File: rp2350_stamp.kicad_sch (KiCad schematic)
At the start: 43 parts, among them J1 Conn_West, J2 Conn_North, J3 Conn_South, J4 Conn_East, Q1 BSS84, SW1 SW_RESET, SW2 SW_BOOTSEL, U1 W25Q128JVPIQ, U2 ME4055, U3 AP2112K-3.3, U4 RP235x-A, Y1 XYDBPCNANF-12MHZ

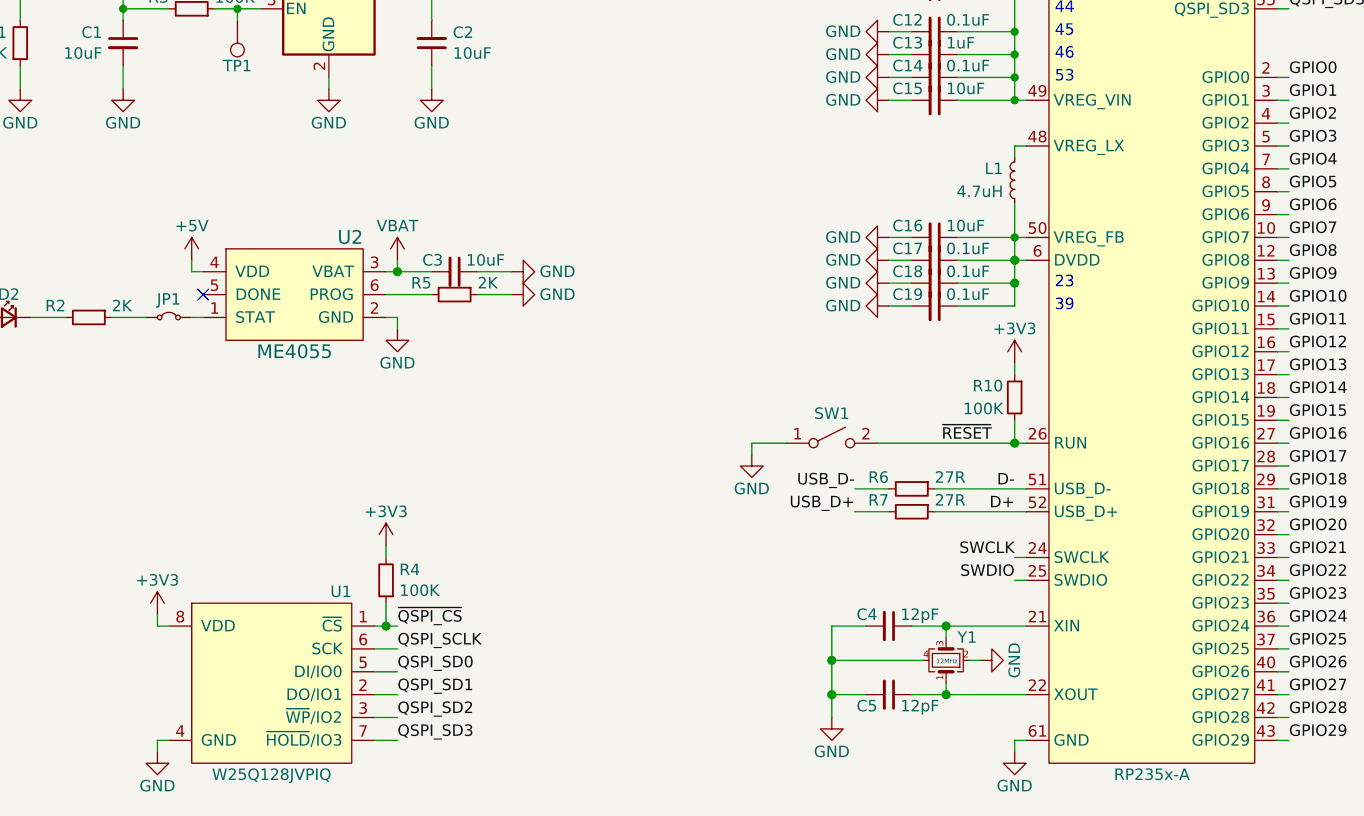
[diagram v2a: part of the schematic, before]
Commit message: Rev 4
- Put chip name on the board
- Fixup pin markers to be uniform
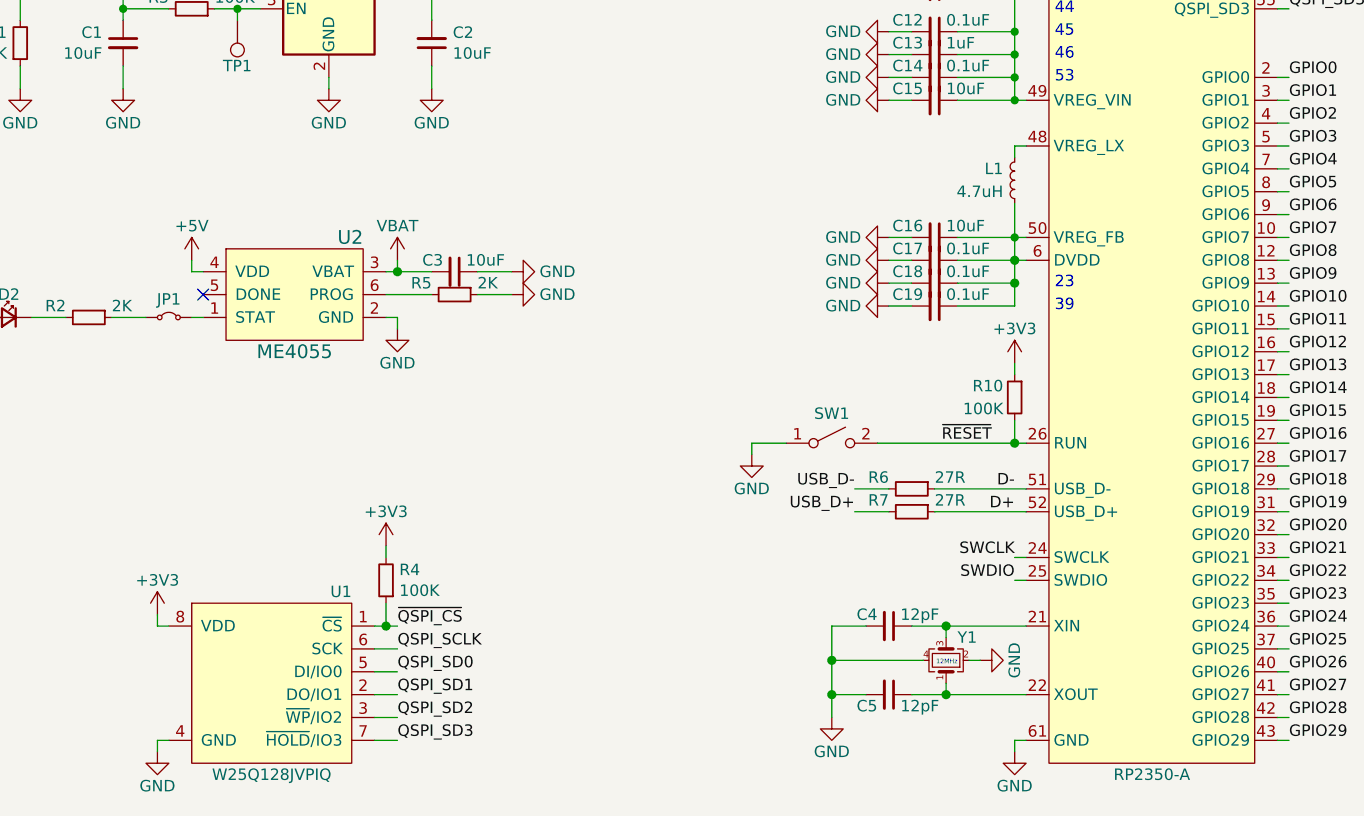
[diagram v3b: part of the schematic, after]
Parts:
- U4: value RP235x-A -> RP2350-A
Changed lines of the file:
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@@
 (kicad_sch
-	(version 20231120)
+	(version 20240602)
 	(generator "eeschema")
-	(generator_version "8.0")
+	(generator_version "8.99")
 	(paper "A4")
 	(title_block
 		(title "RP2350 Stamp")
 	)
+	(text "53"
+		(exclude_from_sim no)
+		(at 146.685 78.74 0)
+		(effects
+			(font
+				(size 1.27 1.27)
+			)
+			(justify left)
+		)
+	)
+	(text "ADC"
+		(exclude_from_sim no)
+		(at 181.61 144.78 0)
+		(effects
+			(font
+				(size 1.27 1.27)
+			)
+			(justify left bottom)
+		)
+	)
+	(text "45"
+		(exclude_from_sim no)
+		(at 146.685 73.66 0)
+		(effects
+			(font
+				(size 1.27 1.27)
+			)
+			(justify left)
+		)
+	)
+	(text "ADC"
+		(exclude_from_sim no)
+		(at 181.61 147.32 0)
+		(effects
+			(font
+				(size 1.27 1.27)
+			)
+			(justify left bottom)
+		)
+	)
+	(text "ADC"
+		(exclude_from_sim no)
+		(at 181.61 149.86 0)
+		(effects
+			(font
+				(size 1.27 1.27)
+			)
+			(justify left bottom)
+		)
+	)
+	(text "39"
+		(exclude_from_sim no)
+		(at 146.685 104.14 0)
+		(effects
+			(font
+				(size 1.27 1.27)
+			)
+			(justify left)
+		)
+	)
+	(text "23"
+		(exclude_from_sim no)
+		(at 146.685 101.6 0)
+		(effects
+			(font
+				(size 1.27 1.27)
+			)
+			(justify left)
+		)
+	)
+	(text "30"
+		(exclude_from_sim no)
+		(at 146.685 66.04 0)
+		(effects
+			(font
+				(size 1.27 1.27)
+			)
+			(justify left)
+		)
+	)
+	(text "20"
+		(exclude_from_sim no)
+		(at 146.685 63.5 0)
+		(effects
+			(font
+				(size 1.27 1.27)
+			)
+			(justify left)
+		)
+	)
+	(text "12MHz"
+		(exclude_from_sim no)
+		(at 135.89 144.145 0)
+		(effects
+			(font
+				(size 0.508 0.508)
+			)
+			(justify right bottom)
+		)
+	)
+	(text "44"
+		(exclude_from_sim no)
+		(at 146.685 71.12 0)
+		(effects
+			(font
+				(size 1.27 1.27)
+			)
+			(justify left)
+		)
+	)
+	(text "46"
+		(exclude_from_sim no)
+		(at 146.685 76.2 0)
+		(effects
+			(font
+				(size 1.27 1.27)
+			)
+			(justify left)
+		)
+	)
+	(text "38"
+		(exclude_from_sim no)
+		(at 146.685 68.58 0)
+		(effects
+			(font
+				(size 1.27 1.27)
+			)
+			(justify left)
+		)
+	)
+	(text "11"
+		(exclude_from_sim no)
+		(at 146.685 60.96 0)
+		(effects
+			(font
+				(size 1.27 1.27)
+			)
+			(justify left)
+		)
+	)
+	(text "ADC"
+		(exclude_from_sim no)
+		(at 181.61 152.4 0)
+		(effects
+			(font
+				(size 1.27 1.27)
+			)
+			(justify left bottom)
+		)
+	)
 	(junction
 		(at 142.24 78.74)
@@
 		)
 	)
-	(text "53"
-		(exclude_from_sim no)
-		(at 146.685 78.74 0)
-		(effects
-			(font
-				(size 1.27 1.27)
-			)
-			(justify left)
-		)
-	)
-	(text "ADC"
-		(exclude_from_sim no)
-		(at 181.61 144.78 0)
-		(effects
-			(font
-				(size 1.27 1.27)
-			)
-			(justify left bottom)
-		)
-	)
-	(text "45"
-		(exclude_from_sim no)
-		(at 146.685 73.66 0)
-		(effects
-			(font
-				(size 1.27 1.27)
-			)
-			(justify left)
-		)
-	)
-	(text "ADC"
-		(exclude_from_sim no)
-		(at 181.61 147.32 0)
-		(effects
-			(font
-				(size 1.27 1.27)
-			)
-			(justify left bottom)
-		)
-	)
-	(text "ADC"
-		(exclude_from_sim no)
-		(at 181.61 149.86 0)
-		(effects
-			(font
-				(size 1.27 1.27)
-			)
-			(justify left bottom)
-		)
-	)
-	(text "39"
-		(exclude_from_sim no)
-		(at 146.685 104.14 0)
-		(effects
-			(font
-				(size 1.27 1.27)
-			)
-			(justify left)
-		)
-	)
-	(text "23"
-		(exclude_from_sim no)
-		(at 146.685 101.6 0)
-		(effects
-			(font
-				(size 1.27 1.27)
-			)
-			(justify left)
-		)
-	)
-	(text "30"
-		(exclude_from_sim no)
-		(at 146.685 66.04 0)
-		(effects
-			(font
-				(size 1.27 1.27)
-			)
-			(justify left)
-		)
-	)
-	(text "20"
-		(exclude_from_sim no)
-		(at 146.685 63.5 0)
-		(effects
-			(font
-				(size 1.27 1.27)
-			)
-			(justify left)
-		)
-	)
-	(text "12MHz"
-		(exclude_from_sim no)
-		(at 135.89 144.145 0)
-		(effects
-			(font
-				(size 0.508 0.508)
-			)
-			(justify right bottom)
-		)
-	)
-	(text "44"
-		(exclude_from_sim no)
-		(at 146.685 71.12 0)
-		(effects
-			(font
-				(size 1.27 1.27)
-			)
-			(justify left)
-		)
-	)
-	(text "46"
-		(exclude_from_sim no)
-		(at 146.685 76.2 0)
-		(effects
-			(font
-				(size 1.27 1.27)
-			)
-			(justify left)
-		)
-	)
-	(text "38"
-		(exclude_from_sim no)
-		(at 146.685 68.58 0)
-		(effects
-			(font
-				(size 1.27 1.27)
-			)
-			(justify left)
-		)
-	)
-	(text "11"
-		(exclude_from_sim no)
-		(at 146.685 60.96 0)
-		(effects
-			(font
-				(size 1.27 1.27)
-			)
-			(justify left)
-		)
-	)
-	(text "ADC"
-		(exclude_from_sim no)
-		(at 181.61 152.4 0)
-		(effects
-			(font
-				(size 1.27 1.27)
-			)
-			(justify left bottom)
-		)
-	)
 	(label "GPIO9"
 		(at 220.98 113.03 180)
@@
 			)
 		)
-		(property "Value" "RP235x-A"
+		(property "Value" "RP2350-A"
 			(at 157.48 156.21 0)
 			(effects

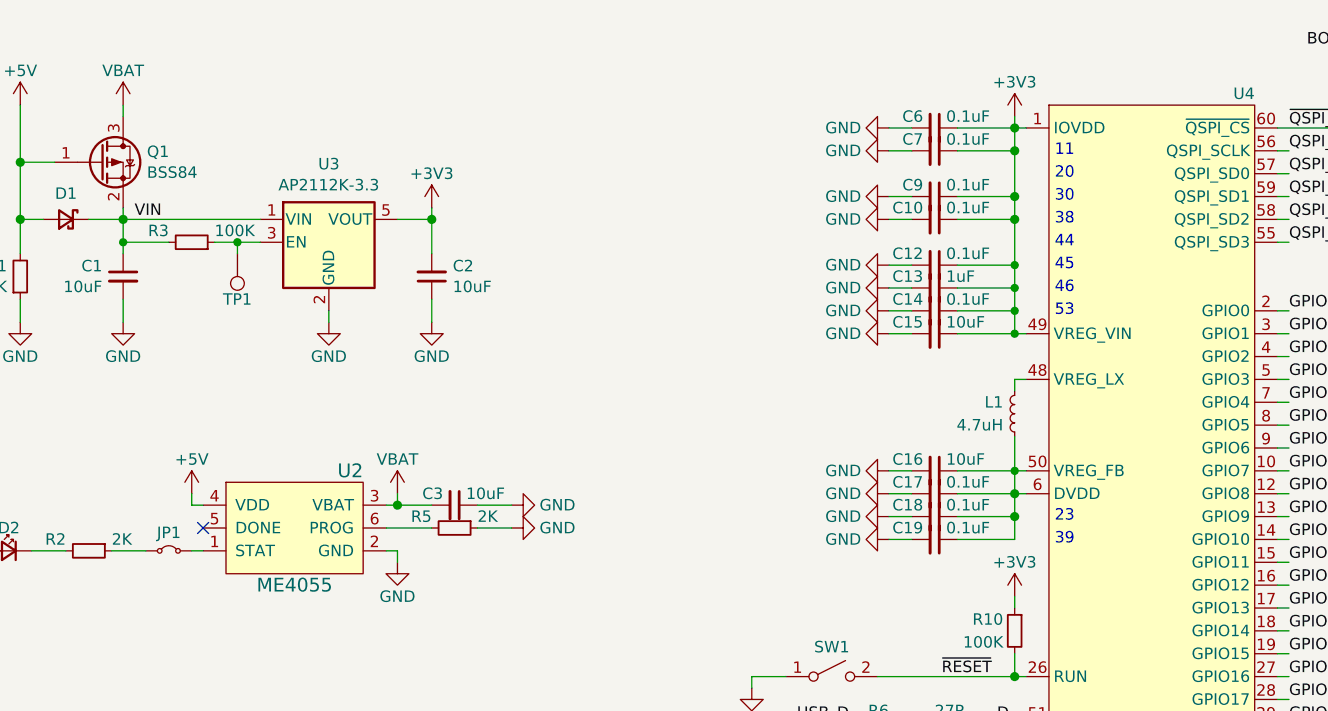
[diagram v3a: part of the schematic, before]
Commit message: Rev 4.5
Fixup power stuff according to RPi's recommendations
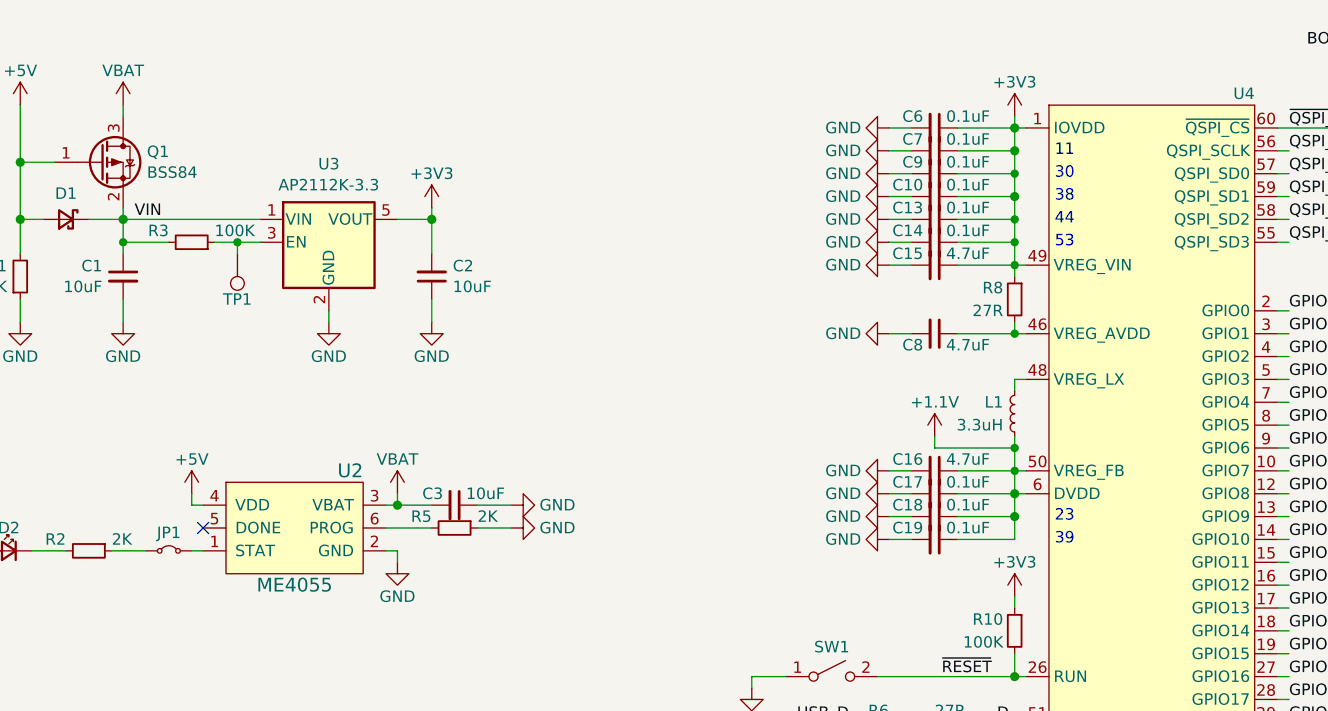
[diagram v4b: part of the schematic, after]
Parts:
- removed C12: 0.1uF, Capacitor_SMD:C_0603_1608Metric, symbol Device:C_Small
- added C8: 4.7uF, Capacitor_SMD:C_0603_1608Metric, symbol Device:C_Small
- added R8: 27R, Resistor_SMD:R_0603_1608Metric, symbol Device:R_Small
- C13: value 1uF -> 0.1uF
- C15, C16: value 10uF -> 4.7uF
- L1: value 4.7uH -> 3.3uH
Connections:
- net +3V3: now also R8.1; no longer U4.46 (IOVDD)
- net GND: now also C8.2
- net +1.1V: now reaches C16.1, C17.1, C18.1, C19.1, L1.1, U4.23 (DVDD), U4.39 (DVDD), U4.50 (VREG_FB), U4.6 (DVDD)
- new net: C8.1, R8.2, U4.46 (VREG_AVDD)
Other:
- note removed: "20"
- note removed: "45"
- note removed: "46"
- moved on the sheet: C10, C13, C14, C15, C9

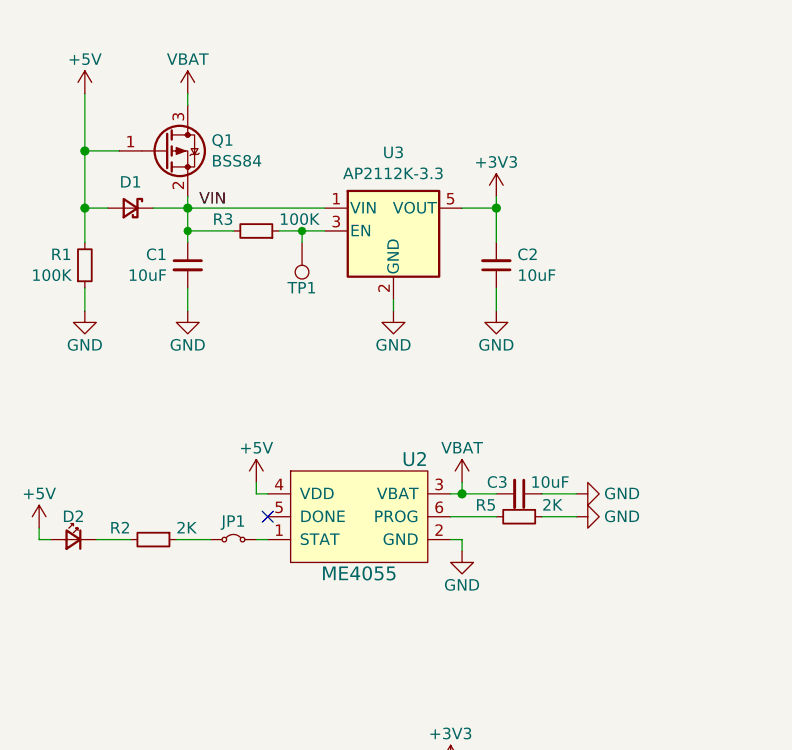
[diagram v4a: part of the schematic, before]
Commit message: Fix BOM info, add README and LICENSE
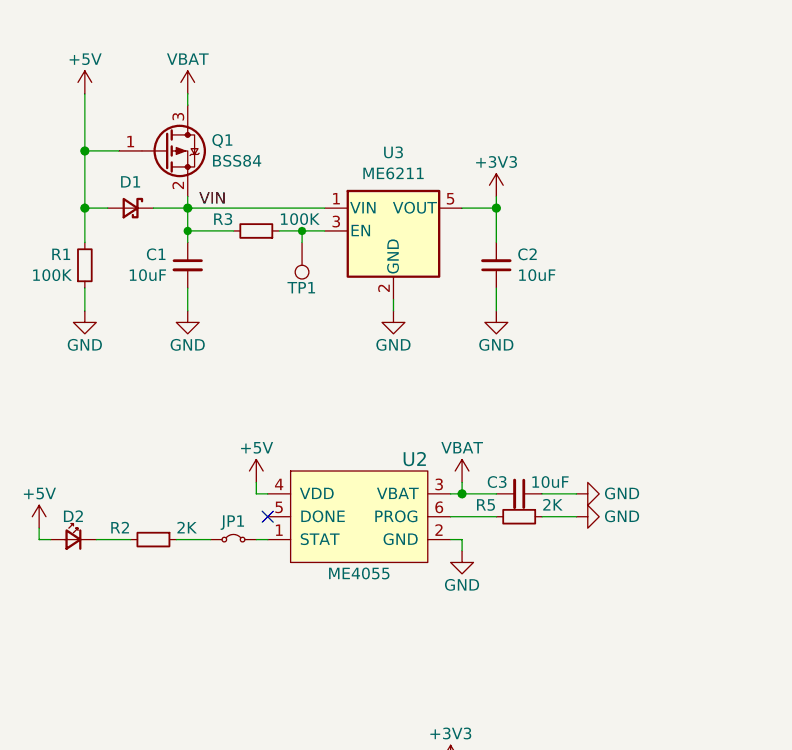
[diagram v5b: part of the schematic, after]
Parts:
- J1, J2, J3, J4: now left out of the parts list
- L1: LCSC C5349608 -> C5832359
- SW1, SW2: LCSC (none) -> C561514
- U3: value AP2112K-3.3 -> ME6211; Digikey AP2112K-3.3TRG1DICT-ND -> (none); LCSC C51118 -> C82942
- Y1: value XYDBPCNANF-12MHZ -> CM4012M00012001; LCSC C521567 -> C7294611
